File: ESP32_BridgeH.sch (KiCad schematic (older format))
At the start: 17 parts, among them J1 MT1, J2 MT2, J3 boot, J4 Serial, SW1 reset, U1 TB6612FNG, U2 ESP32-WROOM, U3 MPU6050, U4 LM7805_TO220

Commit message: foot-print assign to the new elements
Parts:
- added C4: 0.1uF, Capacitor_THT:C_Disc_D4.3mm_W1.9mm_P5.00mm, symbol Device:C
- added VR1: POT, Potentiometer_THT:Potentiometer_Piher_T-16H_Single_Horizontal, symbol freetronics_schematic:POT
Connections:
- net GND: now also D2.2 (A), C4.1, VR1.2
- net Vcc: now also C4.2, VR1.1
- net Vin: now also BT1.1 (+)
- net ADC: now reaches U2.13 (IO14)
- net ADC: now also VR1.W
- no-connect marks 24 -> 23
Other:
- note added: "ADC-POT\n"
- moved on the sheet: D2
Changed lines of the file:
@@
 Wire Wire Line
 	4500 4650 4500 4900
-NoConn ~ 4500 4450
 $Comp
 L power:PWR_FLAG #FLG0101
 U 1 1 5EE4E06E
-P 7350 1600
-F 0 "#FLG0101" H 7350 1675 50  0001 C CNN
-F 1 "PWR_FLAG" H 7350 1773 50  0000 C CNN
-F 2 "" H 7350 1600 50  0001 C CNN
-F 3 "~" H 7350 1600 50  0001 C CNN
-	1    7350 1600
-	1    0    0    -1
-$EndComp
-Text Label 7350 1600 3    50   ~ 0
+P 9150 1550
+F 0 "#FLG0101" H 9150 1625 50  0001 C CNN
+F 1 "PWR_FLAG" H 9150 1723 50  0000 C CNN
+F 2 "" H 9150 1550 50  0001 C CNN
+F 3 "~" H 9150 1550 50  0001 C CNN
+	1    9150 1550
+	1    0    0    -1
+$EndComp
+Text Label 9150 1550 3    50   ~ 0
 Vin
 Wire Notes Line
@@
 L Diode:1N4007 D2
 U 1 1 5ED756C7
-P 9050 4000
-F 0 "D2" H 9050 4216 50  0000 C CNN
-F 1 "1N4007" H 9050 4125 50  0000 C CNN
-F 2 "Diode_THT:D_DO-41_SOD81_P10.16mm_Horizontal" H 9050 3825 50  0001 C CNN
-F 3 "http://www.vishay.com/docs/88503/1n4001.pdf" H 9050 4000 50  0001 C CNN
-	1    9050 4000
-	1    0    0    -1
+P 8950 4500
+F 0 "D2" H 8950 4716 50  0000 C CNN
+F 1 "1N4007" H 8950 4625 50  0000 C CNN
+F 2 "Diode_THT:D_DO-41_SOD81_P10.16mm_Horizontal" H 8950 4325 50  0001 C CNN
+F 3 "http://www.vishay.com/docs/88503/1n4001.pdf" H 8950 4500 50  0001 C CNN
+	1    8950 4500
+	0    1    1    0
 $EndComp
 $Comp
@@
 Wire Wire Line
 	7900 4000 7500 4000
-Wire Wire Line
-	9200 4000 9400 4000
-Wire Wire Line
-	9400 4000 9400 4350
 $Comp
 L power:GND #PWR011
@@
 Text Label 7900 4000 0    50   ~ 0
 Vcc
-Text Label 8850 4000 0    50   ~ 0
+Text Label 8950 4000 0    50   ~ 0
 Vin
-Wire Wire Line
-	8650 4000 8900 4000
 $Comp
 L power:GND #PWR05
@@
 Text Label 3000 1650 0    50   ~ 0
 A02
+Text Label 7900 1750 0    50   ~ 0
+GND
+Wire Wire Line
+	8650 4000 8950 4000
+Wire Wire Line
+	8950 4000 8950 4350
+Wire Wire Line
+	9400 4350 9400 4000
+Wire Wire Line
+	9400 4000 8950 4000
+Connection ~ 8950 4000
+$Comp
+L power:GND #PWR0101
+U 1 1 5EDEDBAA
+P 8950 5200
+F 0 "#PWR0101" H 8950 4950 50  0001 C CNN
+F 1 "GND" H 8955 5027 50  0000 C CNN
+F 2 "" H 8950 5200 50  0001 C CNN
+F 3 "" H 8950 5200 50  0001 C CNN
+	1    8950 5200
+	1    0    0    -1
+$EndComp
+Wire Wire Line
+	8950 4650 8950 5200
+$Comp
+L freetronics_schematic:POT VR1
+U 1 1 5EDF1ECE
+P 7500 1550
+F 0 "VR1" H 7500 1427 50  0000 C CNN
+F 1 "POT" H 7500 1336 50  0000 C CNN
+F 2 "Potentiometer_THT:Potentiometer_Piher_T-16H_Single_Horizontal" H 7500 1550 60  0001 C CNN
+F 3 "" H 7500 1550 60  0000 C CNN
+	1    7500 1550
+	1    0    0    -1
+$EndComp
+Text Label 7050 1750 2    50   ~ 0
+Vcc
+Text Label 4500 4450 2    50   ~ 0
+ADC
+Text Label 7500 1400 2    50   ~ 0
+ADC
 Text Label 7200 3150 3    50   ~ 0
 GND
+Wire Notes Line
+	6750 2400 8200 2400
+Wire Notes Line
+	8200 2400 8200 1150
+Wire Notes Line
+	8200 1150 6750 1150
+Wire Notes Line
+	6750 1150 6750 2400
+Text Notes 6750 1150 0    59   ~ 12
+ADC-POT\n
+$Comp
+L Device:C C4
+U 1 1 5EE0FBE4
+P 7500 1950
+F 0 "C4" V 7752 1950 50  0000 C CNN
+F 1 "0.1uF" V 7661 1950 50  0000 C CNN
+F 2 "Capacitor_THT:C_Disc_D4.3mm_W1.9mm_P5.00mm" H 7538 1800 50  0001 C CNN
+F 3 "~" H 7500 1950 50  0001 C CNN
+	1    7500 1950
+	0    1    1    0
+$EndComp
+Wire Wire Line
+	7250 1550 7250 1750
+Wire Wire Line
+	7250 1950 7350 1950
+Wire Wire Line
+	7750 1550 7750 1750
+Wire Wire Line
+	7750 1950 7650 1950
+Wire Wire Line
+	7250 1750 7050 1750
+Connection ~ 7250 1750
+Wire Wire Line
+	7250 1750 7250 1950
+Wire Wire Line
+	7750 1750 7900 1750
+Connection ~ 7750 1750
+Wire Wire Line
+	7750 1750 7750 1950
 $EndSCHEMATC

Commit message: Routing
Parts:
- removed VR1: POT, Potentiometer_THT:Potentiometer_Piher_T-16H_Single_Horizontal, symbol freetronics_schematic:POT
- added RV1: R_POT, Potentiometer_THT:Potentiometer_Piher_T-16H_Single_Horizontal, symbol Device:R_POT
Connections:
- net ADC: now also RV1.2
- net GND: now also RV1.3
- net Vcc: now also RV1.1
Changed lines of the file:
@@
 Wire Wire Line
 	8950 4650 8950 5200
-$Comp
-L freetronics_schematic:POT VR1
-U 1 1 5EDF1ECE
-P 7500 1550
-F 0 "VR1" H 7500 1427 50  0000 C CNN
-F 1 "POT" H 7500 1336 50  0000 C CNN
-F 2 "Potentiometer_THT:Potentiometer_Piher_T-16H_Single_Horizontal" H 7500 1550 60  0001 C CNN
-F 3 "" H 7500 1550 60  0000 C CNN
-	1    7500 1550
-	1    0    0    -1
-$EndComp
 Text Label 7050 1750 2    50   ~ 0
 Vcc
@@
 Wire Wire Line
 	7750 1750 7750 1950
+$Comp
+L Device:R_POT RV1
+U 1 1 5EE37AC4
+P 7500 1550
+F 0 "RV1" V 7400 1650 50  0000 R CNN
+F 1 "R_POT" V 7300 1650 50  0000 R CNN
+F 2 "Potentiometer_THT:Potentiometer_Piher_T-16H_Single_Horizontal" H 7500 1550 50  0001 C CNN
+F 3 "~" H 7500 1550 50  0001 C CNN
+	1    7500 1550
+	0    -1   -1   0
+$EndComp
+Wire Wire Line
+	7350 1550 7250 1550
+Wire Wire Line
+	7650 1550 7750 1550
 $EndSCHEMATC

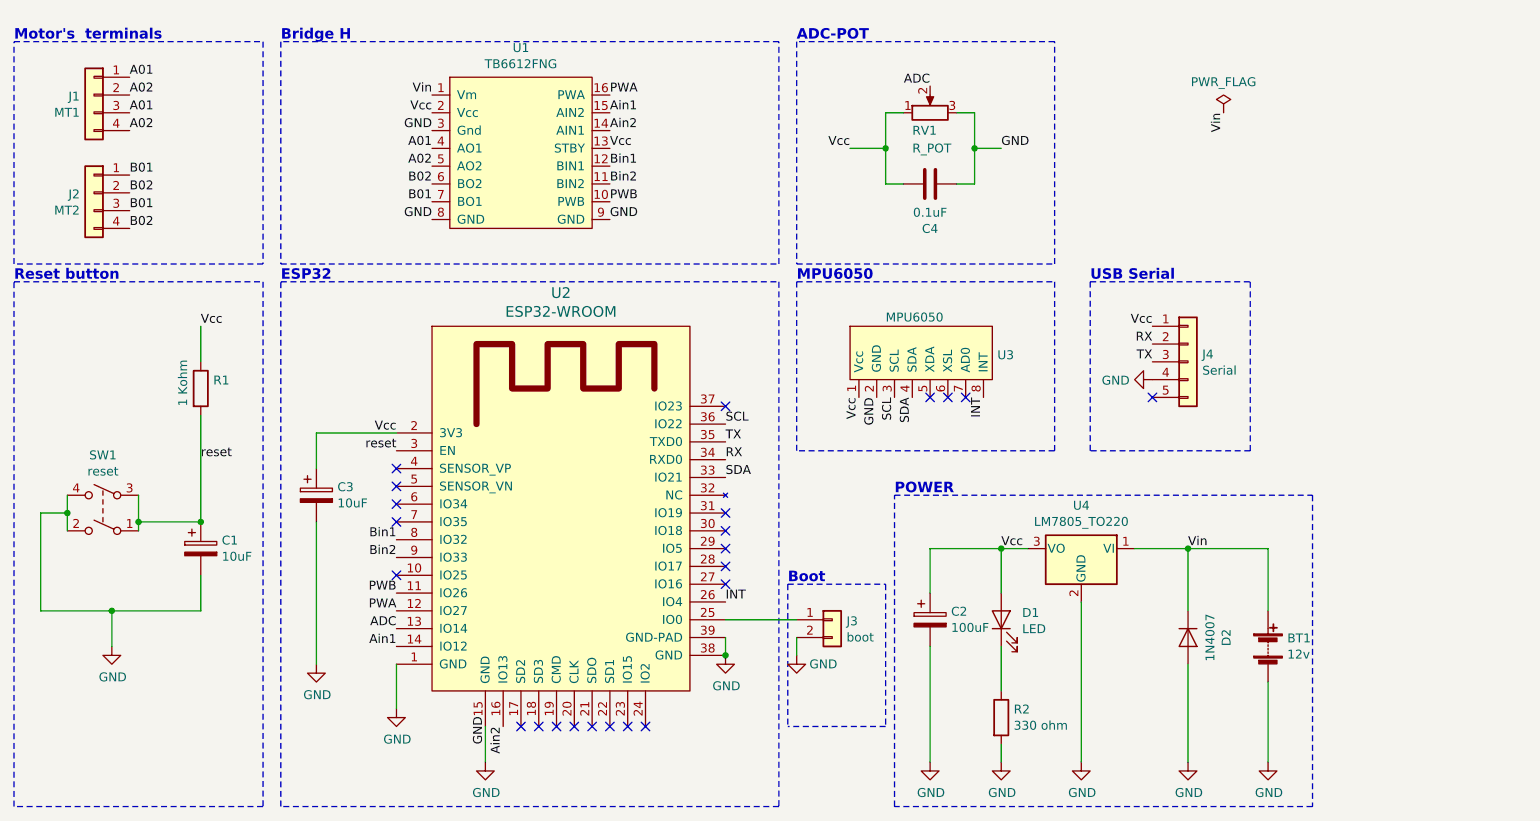
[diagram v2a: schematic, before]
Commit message: Battery reader and boot correction
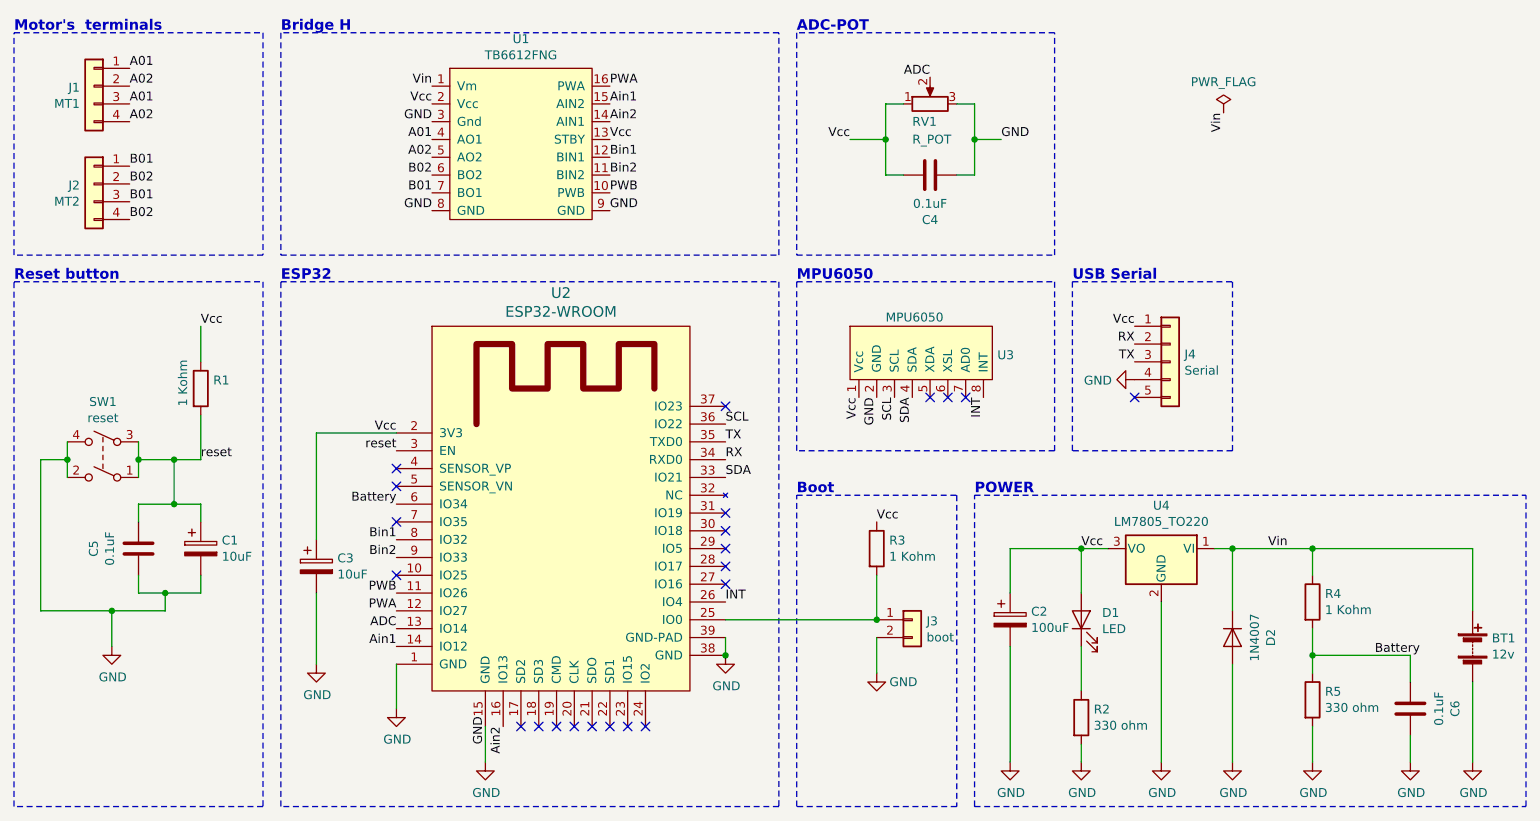
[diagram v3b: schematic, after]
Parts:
- added C5, C6: 0.1uF, Capacitor_THT:C_Disc_D4.3mm_W1.9mm_P5.00mm, symbol Device:C
- added R3, R4: 1 Kohm, Resistor_THT:R_Axial_DIN0207_L6.3mm_D2.5mm_P7.62mm_Horizontal, symbol Device:R
- added R5: 330 ohm, Resistor_THT:R_Axial_DIN0207_L6.3mm_D2.5mm_P7.62mm_Horizontal, symbol Device:R
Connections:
- net GND: now also C5.1, C6.2, R5.2
- net Vcc: now also R3.1
- net Vin: now also R4.1
- net reset: now also C5.2
- net at J3.1 (Pin_1), U2.25 (IO0): now also R3.2
- net Battery: now reaches U2.6 (IO34)
- net Battery: now also C6.1, R4.2, R5.1
- no-connect marks 23 -> 22
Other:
- note added: "Boot"
- note removed: "Boot\n"
- moved on the sheet: BT1, C2, C3, C4, D1, D2, J1, J2, J3, J4, R2, RV1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

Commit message: new footprints without routing
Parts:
- R3, R4, R5: footprint Resistor_THT:R_Axial_DIN0207_L6.3mm_D2.5mm_P7.62mm_Horizontal -> Resistor_THT:R_Axial_DIN0207_L6.3mm_D2.5mm_P5.08mm_Vertical
- SW1: footprint freetronics_footprints:SW_PUSHBUTTON_PTH -> digikey-footprints:Switch_Tactile_THT_6x6mm
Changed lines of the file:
@@
 F 0 "R4" H 9720 4346 50  0000 L CNN
 F 1 "1 Kohm" H 9720 4255 50  0000 L CNN
-F 2 "Resistor_THT:R_Axial_DIN0207_L6.3mm_D2.5mm_P7.62mm_Horizontal" V 9580 4300 50  0001 C CNN
+F 2 "Resistor_THT:R_Axial_DIN0207_L6.3mm_D2.5mm_P5.08mm_Vertical" V 9580 4300 50  0001 C CNN
 F 3 "~" H 9650 4300 50  0001 C CNN
 	1    9650 4300
@@
 F 0 "R5" H 9720 4896 50  0000 L CNN
 F 1 "330 ohm" H 9720 4805 50  0000 L CNN
-F 2 "Resistor_THT:R_Axial_DIN0207_L6.3mm_D2.5mm_P7.62mm_Horizontal" V 9580 4850 50  0001 C CNN
+F 2 "Resistor_THT:R_Axial_DIN0207_L6.3mm_D2.5mm_P5.08mm_Vertical" V 9580 4850 50  0001 C CNN
 F 3 "~" H 9650 4850 50  0001 C CNN
 	1    9650 4850
@@
 F 0 "R3" H 7270 4046 50  0000 L CNN
 F 1 "1 Kohm" H 7270 3955 50  0000 L CNN
-F 2 "Resistor_THT:R_Axial_DIN0207_L6.3mm_D2.5mm_P7.62mm_Horizontal" V 7130 4000 50  0001 C CNN
+F 2 "Resistor_THT:R_Axial_DIN0207_L6.3mm_D2.5mm_P5.08mm_Vertical" V 7130 4000 50  0001 C CNN
 F 3 "~" H 7200 4000 50  0001 C CNN
 	1    7200 4000
@@
 F 0 "SW1" H 2850 3825 50  0000 C CNN
 F 1 "reset" H 2850 3734 50  0000 C CNN
-F 2 "freetronics_footprints:SW_PUSHBUTTON_PTH" H 2850 3500 50  0001 C CNN
+F 2 "digikey-footprints:Switch_Tactile_THT_6x6mm" H 2850 3500 50  0001 C CNN
 F 3 "~" H 2850 3500 50  0001 C CNN
 	1    2850 3500
